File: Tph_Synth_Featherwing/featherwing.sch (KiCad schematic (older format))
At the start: 1 part

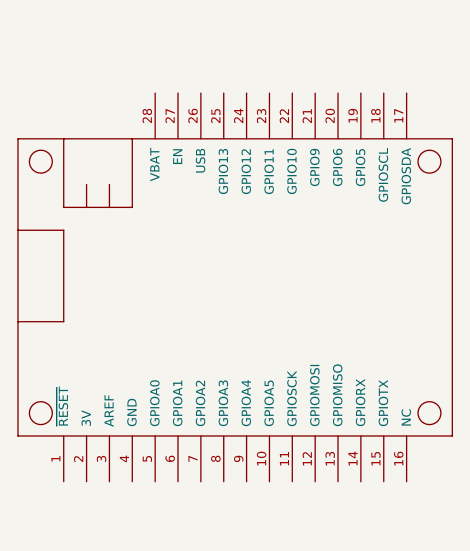
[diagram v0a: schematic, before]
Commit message: Add parts for voltage inverter
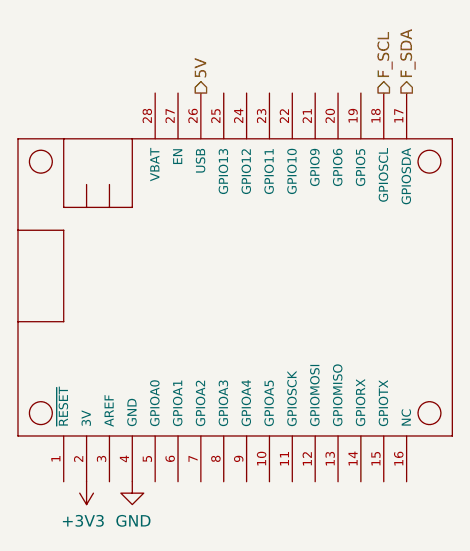
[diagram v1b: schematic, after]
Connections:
- net F_SDA: now reaches MS?.17 (GPIOSDA)
- net F_SCL: now reaches MS?.18 (GPIOSCL)
- net +3V3: now reaches MS?.2 (3V)
- net 5V: now reaches MS?.26 (USB)
- net GND: now reaches MS?.4 (GND)
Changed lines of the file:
@@
 	1    0    0    -1
 $EndComp
+Text HLabel 6390 1870 1    50   Output ~ 0
+F_SCL
+Text HLabel 6490 1870 1    50   Output ~ 0
+F_SDA
+$Comp
+L power:GND #PWR?
+U 1 1 5DECF2D0
+P 5290 3570
+F 0 "#PWR?" H 5290 3320 50  0001 C CNN
+F 1 "GND" H 5295 3397 50  0000 C CNN
+F 2 "" H 5290 3570 50  0001 C CNN
+F 3 "" H 5290 3570 50  0001 C CNN
+	1    5290 3570
+	1    0    0    -1
+$EndComp
+$Comp
+L power:+3V3 #PWR?
+U 1 1 5DECF43D
+P 5090 3570
+F 0 "#PWR?" H 5090 3420 50  0001 C CNN
+F 1 "+3V3" H 5105 3743 50  0000 C CNN
+F 2 "" H 5090 3570 50  0001 C CNN
+F 3 "" H 5090 3570 50  0001 C CNN
+	1    5090 3570
+	-1   0    0    1
+$EndComp
+Text HLabel 5590 1870 1    50   Output ~ 0
+5V
 $EndSCHEMATC

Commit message: Boost-converter and inverting opamps
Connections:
- net VBAT: now reaches MS?.28 (VBAT)
- net 5V renamed VUSB
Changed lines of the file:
@@
 $EndComp
 Text HLabel 5590 1870 1    50   Output ~ 0
-5V
+VUSB
+Text HLabel 5390 1870 1    50   Output ~ 0
+VBAT
 $EndSCHEMATC

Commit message: Added first-cut of schematic
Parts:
- gave numbers to parts that had none: 1
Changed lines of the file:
@@
 $EndDescr
 $Comp
-L adafruit_featherwing:ADAFRUIT_FEATHERWING MS?
+L adafruit_featherwing:ADAFRUIT_FEATHERWING MS1
 U 1 1 5DECFEA6
 P 4790 3370
-F 0 "MS?" H 4790 3370 45  0001 C CNN
+F 0 "MS1" H 4790 3370 45  0001 C CNN
 F 1 "ADAFRUIT_FEATHERWING" H 4790 3370 45  0001 C CNN
 F 2 "" H 4790 3370 50  0001 C CNN

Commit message: Initial attempt at PCB
Signed-off-by: Tisham Dhar <whatnickd@gmail.com>
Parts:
- MS1: footprint (none) -> featherwing:adafruit_featherwing
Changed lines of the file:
@@
 F 0 "MS1" H 4790 3370 45  0001 C CNN
 F 1 "ADAFRUIT_FEATHERWING" H 4790 3370 45  0001 C CNN
-F 2 "" H 4790 3370 50  0001 C CNN
+F 2 "featherwing:adafruit_featherwing" H 4790 3370 50  0001 C CNN
 F 3 "" H 4790 3370 50  0001 C CNN
 	1    4790 3370

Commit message: Added BOM and upgraded to kicad 5.0
Signed-off-by: Tisham Dhar <whatnickd@gmail.com>
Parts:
- MS1: manf# (none) -> 3200
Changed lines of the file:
@@
 EESchema Schematic File Version 4
-LIBS:Tph_Synth_Featherwing-cache
-EELAYER 26 0
+EELAYER 30 0
 EELAYER END
 $Descr A4 11693 8268
@@
 F 2 "featherwing:adafruit_featherwing" H 4790 3370 50  0001 C CNN
 F 3 "" H 4790 3370 50  0001 C CNN
+F 4 "3200" H 4790 3370 50  0001 C CNN "manf#"
 	1    4790 3370
 	1    0    0    -1

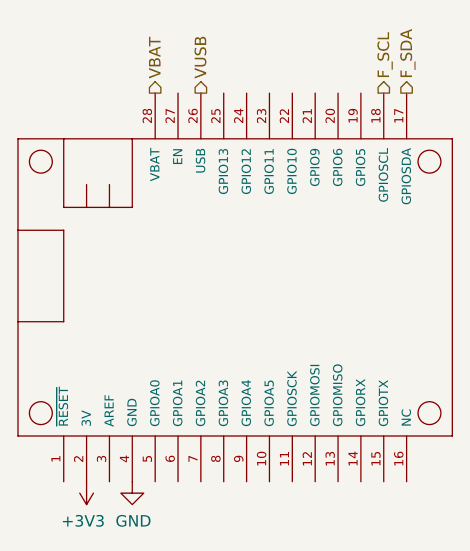
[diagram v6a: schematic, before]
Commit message: #1 and #2 add mising wiring
Signed-off-by: Tisham Dhar <whatnickd@gmail.com>
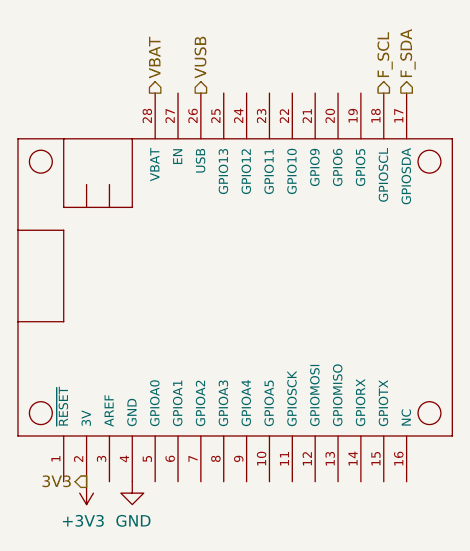
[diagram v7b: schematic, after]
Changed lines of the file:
@@
 Text HLabel 5390 1870 1    50   Output ~ 0
 VBAT
+Text HLabel 5090 3570 0    50   Output ~ 0
+3V3
 $EndSCHEMATC
